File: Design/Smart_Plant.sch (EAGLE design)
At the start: 67 parts, among them IC1 AMS1117-3.3, IC2 TLC555CDR, IC3 AHT20, IC4 TP4056, J2 USBC-6P, Q1 IRLML0100, Q2 ALS-PT19-315C, T1 MMBT2222A, T2 LBSS84LT1G, U1 ESP-32S

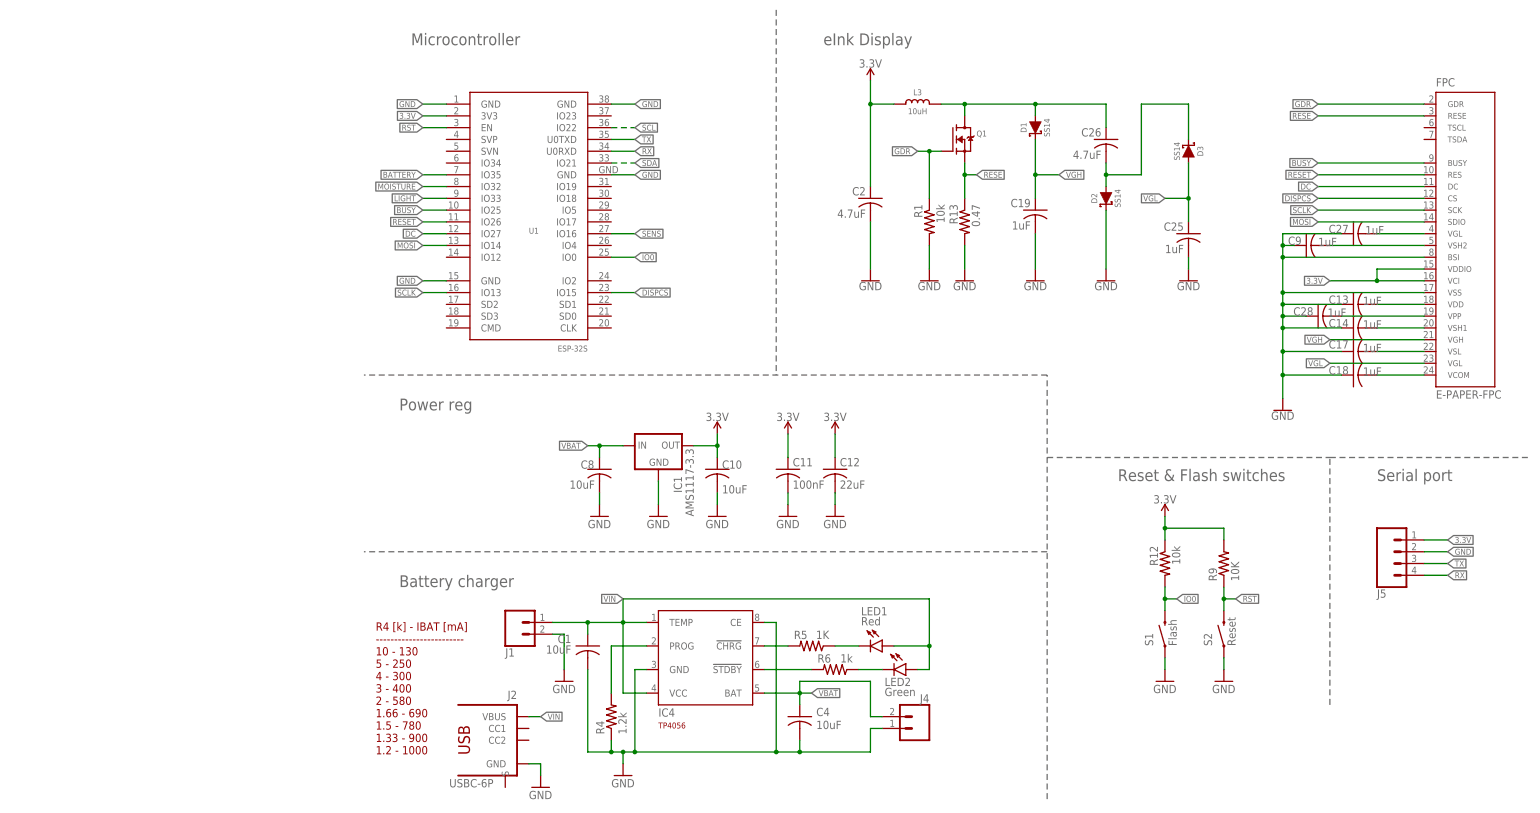
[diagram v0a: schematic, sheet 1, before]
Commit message: Added power patch
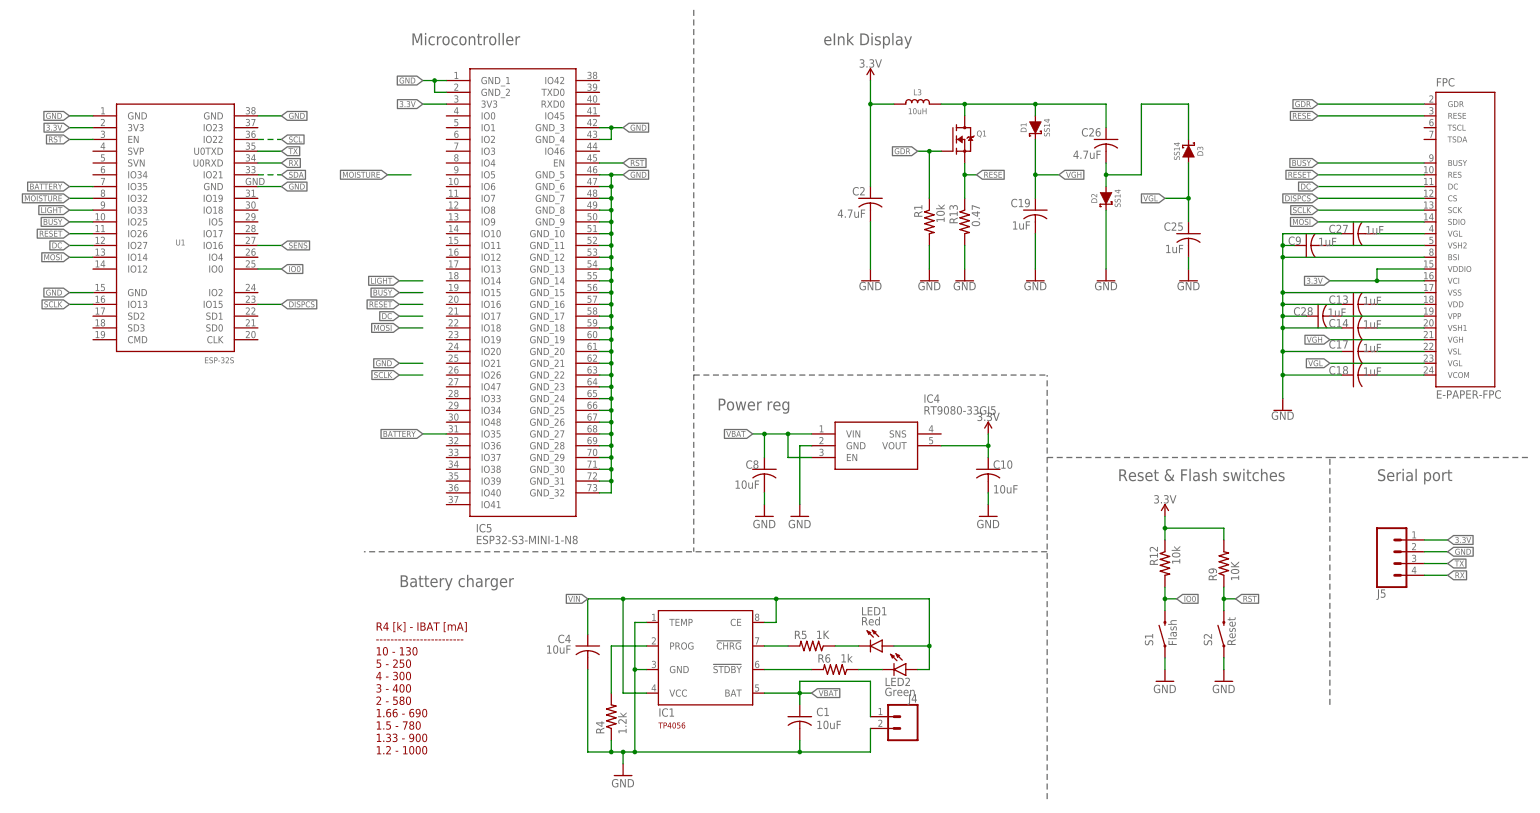
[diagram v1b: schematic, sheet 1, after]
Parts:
- removed C11: 100nF, rcl:C-USC0603
- removed C12: 22uF, rcl:C-USC0603
- removed J2: USBC-6P, SpaceDIY_connectors:USBC-6P
- added D5, D6: B340A-13-F, SamacSys_Parts:B340A-13-F
- added IC5: ESP32-S3-MINI-1-N8, SamacSys_Parts:ESP32-S3-MINI-1-N8
- added J6: USB-C, SparkFun-Connectors:USB_C_4-LAYER-ISOLATED
- added R28, R29: 5.1k, rcl:R-US_R0603
- IC1: value AMS1117-3.3 -> TP4056; device SparkFun-IC-Power:V_REG_LD1117VXXLD1117-SMD -> TP4056:TP4056
- IC4: value TP4056 -> RT9080-33GJ5; device TP4056:TP4056 -> SamacSys_Parts:RT9080-33GJ5; LCSC (none) -> C841192
- J4: device SparkFun-Connectors:CONN_02-JST-2-PTH-NO_SILK -> SpaceDIY_connectors:CONN_02-JST-2MM-SMT; LCSC (none) -> C3029440
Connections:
- removed net N$2 (its old number): IC4.!STDBY, R6.2
- new net CC1: J6.CC2, R28.2
- new net CC2: J6.CC1, R29.2
- new net D+: J6.D+
- new net D-: J6.D-
- new net N$35: D6.A, J1.1
- new net N$4: IC1.PROG, R4.2
- new net V_USB: D5.A, J6.VBUS
- net 3.3V: now also IC4.VOUT, IC5.3V3; no longer C11.1, C12.1, IC1.OUT
- net BATTERY: now also IC5.IO35
- net GND: now also IC1.TEMP, IC5.GND_1, IC5.GND_10, IC5.GND_11, IC5.GND_12, IC5.GND_13, IC5.GND_14, IC5.GND_15, IC5.GND_16, IC5.GND_17, IC5.GND_18, IC5.GND_19, IC5.GND_2, IC5.GND_20, IC5.GND_21, IC5.GND_22, IC5.GND_23, IC5.GND_24, IC5.GND_25, IC5.GND_26, IC5.GND_27, IC5.GND_28, IC5.GND_29, IC5.GND_3, IC5.GND_30, IC5.GND_31, IC5.GND_32, IC5.GND_4, IC5.GND_5, IC5.GND_6, IC5.GND_7, IC5.GND_8, IC5.GND_9, J6.GND, R28.1, R29.1; no longer C11.2, C12.2, IC4.CE, J2.GND
- net N$1: now also IC1.!STDBY, R6.2; no longer IC4.PROG, R4.2
- net N$6: now also IC1.!CHRG; no longer IC4.!CHRG
- net RST: now also IC5.EN
- net VBAT: now also C1.1, IC1.BAT, IC4.EN, IC4.VIN; no longer C4.1, IC1.IN, IC4.BAT
- net VIN: now also C4.1, D5.K, D6.K, IC1.CE, IC1.VCC; no longer C1.1, IC4.TEMP, IC4.VCC, J1.1, J2.VBUS
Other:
- note added: "Input power/data connectors"
- moved on the sheet: C1, C10, C4, C8, J4, Q2, R10, R11, R14, R18, R19, T1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
